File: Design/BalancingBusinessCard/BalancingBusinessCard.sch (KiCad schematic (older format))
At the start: 1 part

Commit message: Made a part
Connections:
- net SDA: now reaches U?.1 (PB0)
- net ADC1: now reaches U?.19 (PA1)
- net ADC0: now reaches U?.20 (PA0)
- net SCL: now reaches U?.3 (PB2)
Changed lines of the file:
@@
 $EndComp
-$Sheet
-S 7500 2300 1600 1200
-U 5BCB9BF4
-F0 "LightModule" 50
-F1 "lightModule.sch" 50
-$EndSheet
 $Sheet
 S 7500 3700 1600 1200
@@
 F1 "motorModule.sch" 50
 $EndSheet
+$Sheet
+S 7500 2300 1600 1200
+U 5BCB9BF4
+F0 "LightModule" 50
+F1 "lightModule.sch" 50
+F2 "LED_1" I L 7500 2600 50
+F3 "LED_2" I L 7500 2700 50
+F4 "LED_3" I L 7500 2800 50
+F5 "LED_4" I L 7500 2900 50
+F6 "LED_5" I L 7500 3000 50
+F7 "LED_6" I L 7500 3100 50
+F8 "LED_7" I L 7500 3200 50
+F9 "LED_0" I L 7500 2500 50
+F10 "LED_8" I L 7500 3300 50
+$EndSheet
+Text Label 3800 2950 0    50   ~ 0
+ADC0
+Text Label 3800 3050 0    50   ~ 0
+ADC1
+Text Label 3800 3850 0    50   ~ 0
+SDA
+Text Label 3800 4050 0    50   ~ 0
+SCL
 $EndSCHEMATC

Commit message: Fixed reference
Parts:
- U?: symbol MCU_Microchip_ATtiny:ATtiny261-20SU -> MCU_Microchip_ATtiny:ATtiny261A-SU
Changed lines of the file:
@@
 EESchema Schematic File Version 4
+LIBS:BalancingBusinessCard-cache
 EELAYER 26 0
 EELAYER END
@@
 $EndDescr
 $Comp
-L MCU_Microchip_ATtiny:ATtiny261-20SU U?
+L MCU_Microchip_ATtiny:ATtiny261A-SU U?
 U 1 1 5BCB9B43
 P 3100 3750

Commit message: Made more parts
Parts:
- added BT?: Battery, symbol Device:Battery
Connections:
- new net +BATT: BT?.1 (+)
- new net GND: BT?.2 (-)
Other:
- note added: "+3V"
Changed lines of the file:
@@
 EESchema Schematic File Version 4
-LIBS:BalancingBusinessCard-cache
 EELAYER 26 0
 EELAYER END
@@
 F0 "MotorModule" 50
 F1 "motorModule.sch" 50
+F2 "DIFF1" I L 7500 3800 50
+F3 "DIFF2" I L 7500 3900 50
+F4 "INA" I L 7500 4000 50
+F5 "INB" I L 7500 4100 50
+F6 "VC" I L 7500 4200 50
+F7 "VM" I L 7500 4300 50
 $EndSheet
 $Sheet
@@
 Text Label 3800 4050 0    50   ~ 0
 SCL
+$Comp
+L Device:Battery BT?
+U 1 1 5BCBEFF8
+P 4400 1300
+F 0 "BT?" H 4508 1346 50  0000 L CNN
+F 1 "Battery" H 4508 1255 50  0000 L CNN
+F 2 "" V 4400 1360 50  0001 C CNN
+F 3 "~" V 4400 1360 50  0001 C CNN
+	1    4400 1300
+	1    0    0    -1
+$EndComp
+$Comp
+L power:+BATT #PWR?
+U 1 1 5BCBF44A
+P 4400 1100
+F 0 "#PWR?" H 4400 950 50  0001 C CNN
+F 1 "+BATT" H 4415 1273 50  0000 C CNN
+F 2 "" H 4400 1100 50  0001 C CNN
+F 3 "" H 4400 1100 50  0001 C CNN
+	1    4400 1100
+	1    0    0    -1
+$EndComp
+Text Notes 4600 950  0    50   ~ 0
++3V
+$Comp
+L power:GND #PWR?
+U 1 1 5BCBF4A9
+P 4400 1500
+F 0 "#PWR?" H 4400 1250 50  0001 C CNN
+F 1 "GND" H 4405 1327 50  0000 C CNN
+F 2 "" H 4400 1500 50  0001 C CNN
+F 3 "" H 4400 1500 50  0001 C CNN
+	1    4400 1500
+	1    0    0    -1
+$EndComp
+$Comp
+L power:+BATT #PWR?
+U 1 1 5BCBF62A
+P 7050 4300
+F 0 "#PWR?" H 7050 4150 50  0001 C CNN
+F 1 "+BATT" H 7065 4473 50  0000 C CNN
+F 2 "" H 7050 4300 50  0001 C CNN
+F 3 "" H 7050 4300 50  0001 C CNN
+	1    7050 4300
+	1    0    0    -1
+$EndComp
+Wire Wire Line
+	7050 4300 7500 4300
 $EndSCHEMATC

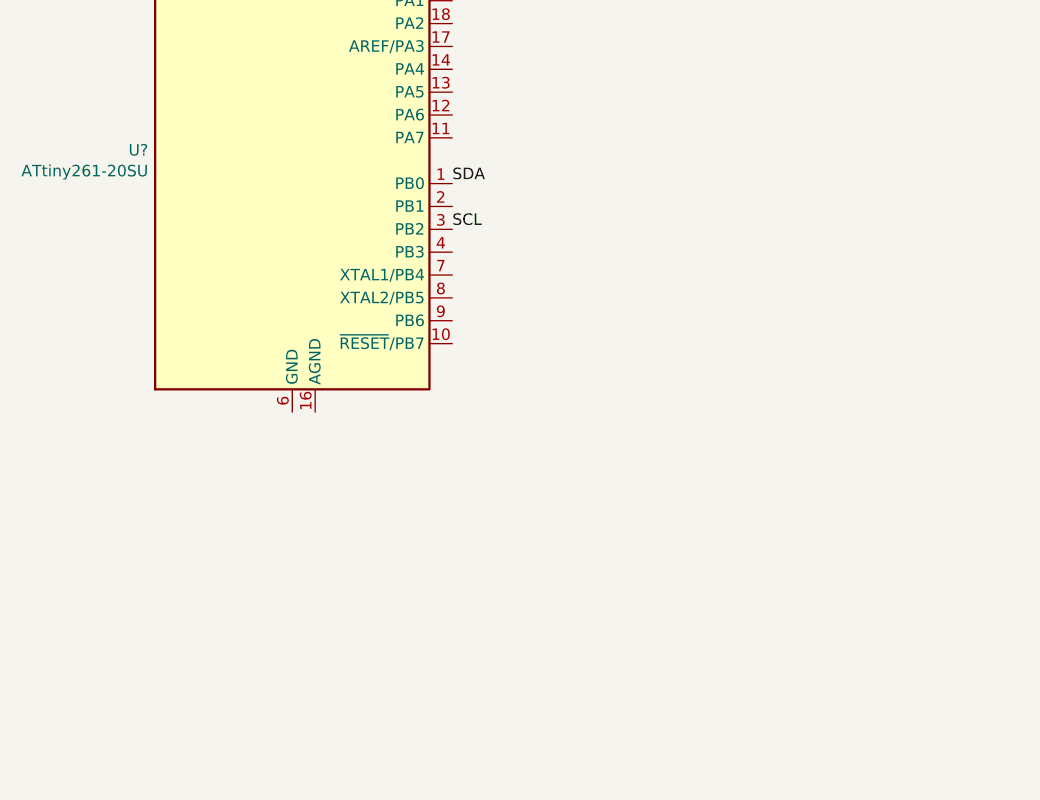
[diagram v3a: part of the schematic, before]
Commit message: Added ICSP header
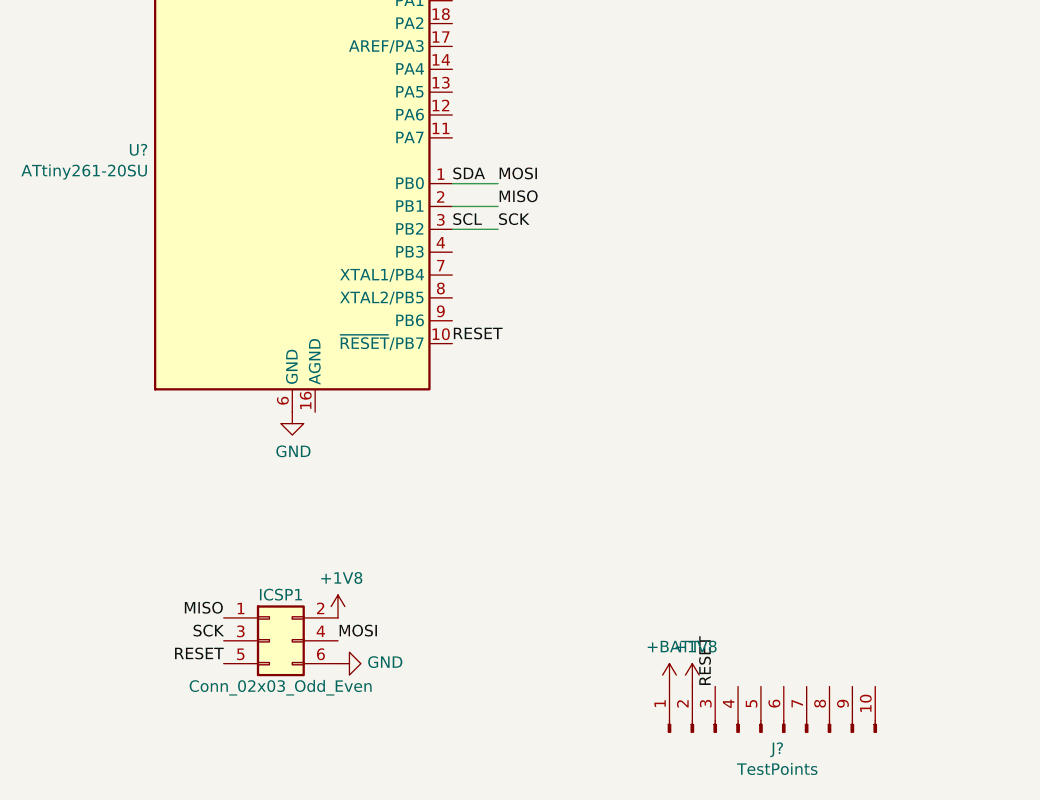
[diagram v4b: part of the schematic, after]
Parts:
- added ICSP1: Conn_02x03_Odd_Even, Connector_PinHeader_2.54mm:PinHeader_2x03_P2.54mm_Vertical, symbol Connector_Generic:Conn_02x03_Odd_Even
- added J?: TestPoints, Connector_PinHeader_2.54mm:PinHeader_1x10_P2.54mm_Vertical, symbol Connector:Conn_01x10_Male
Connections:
- net +BATT: now also J?.1 (Pin_1)
- net GND: now also U?.6 (GND), ICSP1.6 (Pin_6)
- net RESET: now reaches U?.10 (~RESET~/PB7)
- net RESET: now also ICSP1.5 (Pin_5), J?.3 (Pin_3)
- net MISO: now reaches U?.2 (PB1)
- net MISO: now also ICSP1.1 (Pin_1)
- net SCL renamed SCK
- net SCK: now also ICSP1.3 (Pin_3)
- net SDA renamed MOSI
- net MOSI: now also ICSP1.4 (Pin_4)
- new net +1V8: ICSP1.2 (Pin_2), J?.2 (Pin_2)
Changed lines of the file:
@@
 EESchema Schematic File Version 4
+LIBS:BalancingBusinessCard-cache
 EELAYER 26 0
 EELAYER END
@@
 Wire Wire Line
 	7050 4300 7500 4300
+$Comp
+L Connector_Generic:Conn_02x03_Odd_Even ICSP1
+U 1 1 5BCBEC7A
+P 3000 5850
+F 0 "ICSP1" H 3050 6050 50  0000 C CNN
+F 1 "Conn_02x03_Odd_Even" H 3050 5650 50  0000 C CNN
+F 2 "Connector_PinHeader_2.54mm:PinHeader_2x03_P2.54mm_Vertical" H 3000 5850 50  0001 C CNN
+F 3 "~" H 3000 5850 50  0001 C CNN
+	1    3000 5850
+	1    0    0    -1
+$EndComp
+Text Label 3300 5850 0    50   ~ 0
+MOSI
+$Comp
+L power:+1V8 #PWR?
+U 1 1 5BCBF021
+P 3300 5750
+F 0 "#PWR?" H 3300 5600 50  0001 C CNN
+F 1 "+1V8" H 3315 5923 50  0000 C CNN
+F 2 "" H 3300 5750 50  0001 C CNN
+F 3 "" H 3300 5750 50  0001 C CNN
+	1    3300 5750
+	1    0    0    -1
+$EndComp
+$Comp
+L Connector:Conn_01x10_Male J?
+U 1 1 5BCBF241
+P 5150 6250
+F 0 "J?" V 5078 6177 50  0000 C CNN
+F 1 "TestPoints" V 4987 6177 50  0000 C CNN
+F 2 "Connector_PinHeader_2.54mm:PinHeader_1x10_P2.54mm_Vertical" H 5150 6250 50  0001 C CNN
+F 3 "~" H 5150 6250 50  0001 C CNN
+	1    5150 6250
+	0    -1   -1   0
+$EndComp
+$Comp
+L power:+1V8 #PWR?
+U 1 1 5BCBF527
+P 4850 6050
+F 0 "#PWR?" H 4850 5900 50  0001 C CNN
+F 1 "+1V8" H 4865 6223 50  0000 C CNN
+F 2 "" H 4850 6050 50  0001 C CNN
+F 3 "" H 4850 6050 50  0001 C CNN
+	1    4850 6050
+	1    0    0    -1
+$EndComp
+$Comp
+L power:+BATT #PWR?
+U 1 1 5BCBF6B8
+P 4750 6050
+F 0 "#PWR?" H 4750 5900 50  0001 C CNN
+F 1 "+BATT" H 4765 6223 50  0000 C CNN
+F 2 "" H 4750 6050 50  0001 C CNN
+F 3 "" H 4750 6050 50  0001 C CNN
+	1    4750 6050
+	1    0    0    -1
+$EndComp
+$Comp
+L power:GND #PWR?
+U 1 1 5BCBF839
+P 3300 5950
+F 0 "#PWR?" H 3300 5700 50  0001 C CNN
+F 1 "GND" V 3305 5822 50  0000 R CNN
+F 2 "" H 3300 5950 50  0001 C CNN
+F 3 "" H 3300 5950 50  0001 C CNN
+	1    3300 5950
+	0    -1   -1   0
+$EndComp
+Text Label 2800 5750 2    50   ~ 0
+MISO
+Text Label 2800 5850 2    50   ~ 0
+SCK
+Text Label 2800 5950 2    50   ~ 0
+RESET
+Text Label 3800 4550 0    50   ~ 0
+RESET
+Text Label 4950 6050 1    50   ~ 0
+RESET
+$Comp
+L power:GND #PWR?
+U 1 1 5BCCA97D
+P 3100 4850
+F 0 "#PWR?" H 3100 4600 50  0001 C CNN
+F 1 "GND" H 3105 4677 50  0000 C CNN
+F 2 "" H 3100 4850 50  0001 C CNN
+F 3 "" H 3100 4850 50  0001 C CNN
+	1    3100 4850
+	1    0    0    -1
+$EndComp
+Text Label 4000 3850 0    50   ~ 0
+MOSI
+Wire Wire Line
+	4000 3850 3800 3850
+Text Label 4000 3950 0    50   ~ 0
+MISO
+Text Label 4000 4050 0    50   ~ 0
+SCK
+Wire Wire Line
+	4000 4050 3800 4050
+Wire Wire Line
+	4000 3950 3800 3950
 $EndSCHEMATC

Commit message: Added IMU
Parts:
- added R? (x2): 1k, symbol Device:R
- J?: footprint Connector_PinHeader_2.54mm:PinHeader_1x10_P2.54mm_Vertical -> CustomFootprints:Testpoint_1x10
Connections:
- net +1V8: now also R?.1, R?.1
- net MOSI: now also R?.2
- net SCK: now also R?.2
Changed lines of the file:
@@
 $Descr A4 11693 8268
 encoding utf-8
-Sheet 1 3
+Sheet 1 4
 Title ""
 Date ""
@@
 F 0 "J?" V 5078 6177 50  0000 C CNN
 F 1 "TestPoints" V 4987 6177 50  0000 C CNN
-F 2 "Connector_PinHeader_2.54mm:PinHeader_1x10_P2.54mm_Vertical" H 5150 6250 50  0001 C CNN
+F 2 "CustomFootprints:Testpoint_1x10" H 5150 6250 50  0001 C CNN
 F 3 "~" H 5150 6250 50  0001 C CNN
 	1    5150 6250
@@
 Wire Wire Line
 	4000 3950 3800 3950
+$Sheet
+S 7500 950  1600 1100
+U 5BCBF6E4
+F0 "Accelerometer" 50
+F1 "LIS3DHTR.sch" 50
+F2 "SDA" I L 7500 1300 50
+F3 "SCL" I L 7500 1400 50
+$EndSheet
+Text Label 7300 1300 2    50   ~ 0
+SDA
+Text Label 7050 1400 2    50   ~ 0
+SCL
+Wire Wire Line
+	7500 1300 7350 1300
+$Comp
+L Device:R R?
+U 1 1 5BCC12E2
+P 7350 1150
+F 0 "R?" H 7420 1196 50  0000 L CNN
+F 1 "1k" H 7420 1105 50  0000 L CNN
+F 2 "" V 7280 1150 50  0001 C CNN
+F 3 "~" H 7350 1150 50  0001 C CNN
+	1    7350 1150
+	1    0    0    -1
+$EndComp
+Wire Wire Line
+	7300 1300 7350 1300
+Connection ~ 7350 1300
+$Comp
+L power:+1V8 #PWR?
+U 1 1 5BCC13E8
+P 7200 1000
+F 0 "#PWR?" H 7200 850 50  0001 C CNN
+F 1 "+1V8" H 7215 1173 50  0000 C CNN
+F 2 "" H 7200 1000 50  0001 C CNN
+F 3 "" H 7200 1000 50  0001 C CNN
+	1    7200 1000
+	1    0    0    -1
+$EndComp
+Wire Wire Line
+	7350 1000 7200 1000
+Wire Wire Line
+	7200 1000 7100 1000
+Connection ~ 7200 1000
+$Comp
+L Device:R R?
+U 1 1 5BCC14CF
+P 7100 1250
+F 0 "R?" H 6950 1350 50  0000 L CNN
+F 1 "1k" H 6950 1250 50  0000 L CNN
+F 2 "" V 7030 1250 50  0001 C CNN
+F 3 "~" H 7100 1250 50  0001 C CNN
+	1    7100 1250
+	1    0    0    -1
+$EndComp
+Wire Wire Line
+	7100 1000 7100 1100
+Wire Wire Line
+	7050 1400 7100 1400
+Wire Wire Line
+	7100 1400 7500 1400
+Connection ~ 7100 1400
 $EndSCHEMATC
